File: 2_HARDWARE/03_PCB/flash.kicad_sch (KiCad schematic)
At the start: 8 parts, among them U15 W25Q128JVSIQ, U16 W25Q128JVSIQ

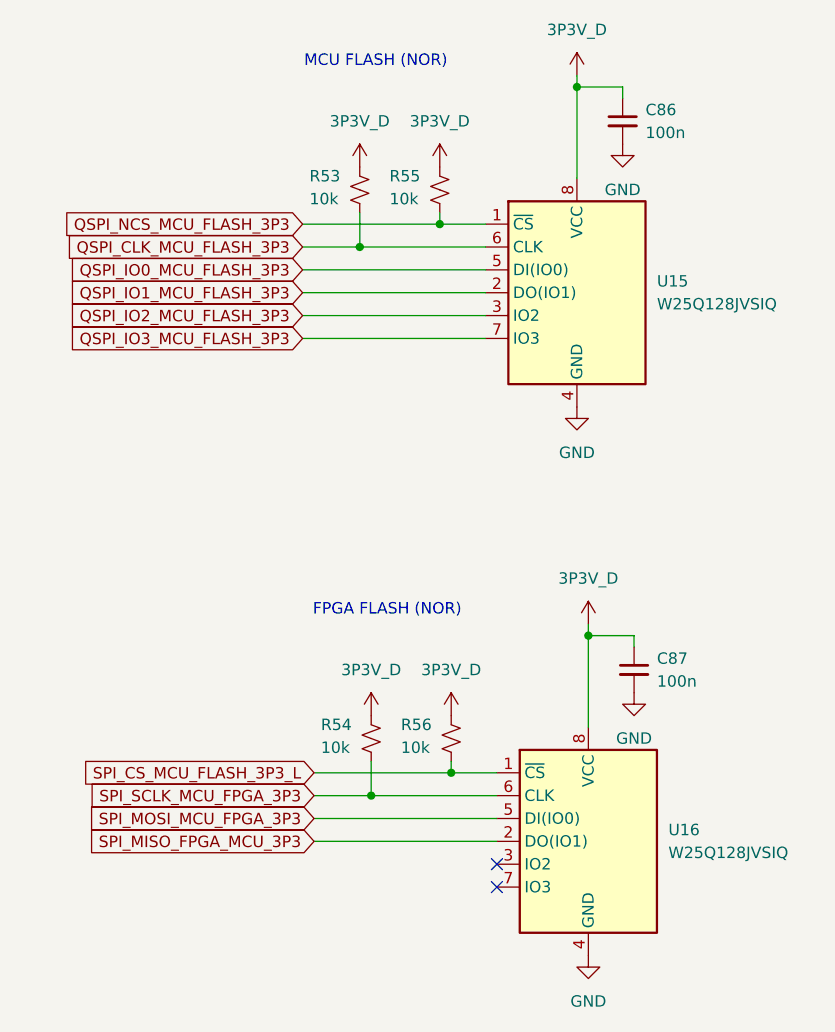
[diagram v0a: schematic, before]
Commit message: MINOR: Changed Boot Select Switches to Pull-Downs / Pull Up DNI and continued layout.
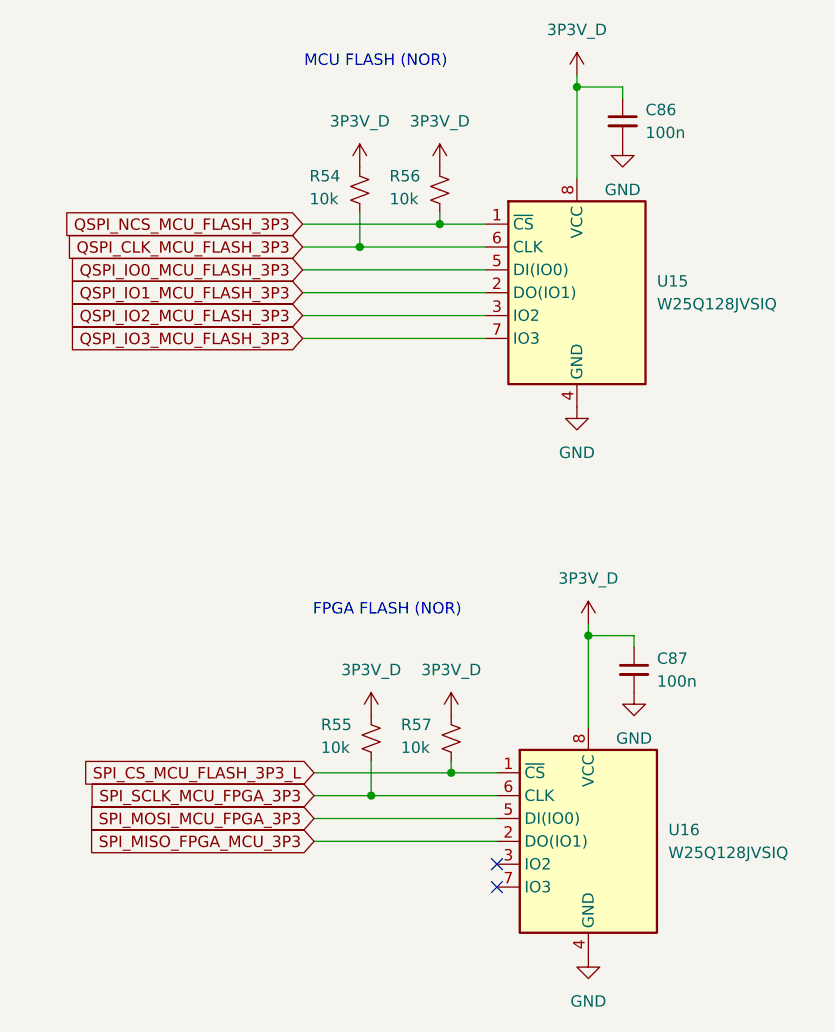
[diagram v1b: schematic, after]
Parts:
- renumbered R53 to R54, R54 to R55, R55 to R56, R56 to R57
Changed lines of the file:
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@@
+		(dnp no)
+		(fields_autoplaced yes)
+		(property "Reference" "#PWR0207"
+			(at 156.21 105.41 0)
+			(effects
+				(font
+					(size 1.27 1.27)
+				)
+				(hide yes)
+			)
+		)
+		(property "Value" "GND"
+			(at 156.21 104.14 0)
+			(effects
+				(font
+					(size 1.27 1.27)
+				)
+			)
+		)
+		(property "Footprint" ""
+			(at 156.21 99.06 0)
+			(effects
+				(font
+					(size 1.27 1.27)
+				)
+				(hide yes)
+			)
+		)
+		(property "Datasheet" ""
+			(at 156.21 99.06 0)
+			(effects
+				(font
+					(size 1.27 1.27)
+				)
+				(hide yes)
+			)
+		)
+		(property "Description" "Power symbol creates a global label with name \"GND\" , ground"
+			(at 156.21 99.06 0)
+			(effects
+				(font
+					(size 1.27 1.27)
+				)
+				(hide yes)
+			)
+		)
+		(pin "1"
+		)
+		(instances
+			(project "arb"
+				(path "/866ef9be-3b01-4288-a6e0-a2357aa17e50/3eaf535e-ef91-4de7-bf25-42486b2f88fe"
+					(reference "#PWR0207")
+					(unit 1)
+				)
+			)
+		)
+	)
+	(symbol
+		(lib_id "Device:R_Small_US")
+		(at 133.35 135.89 180)
+		(unit 1)
+		(exclude_from_sim no)
+		(in_bom yes)
+		(on_board yes)
+		(dnp no)
+		(property "Reference" "R55"
+			(at 127.762 134.366 0)
+			(effects
+				(font
+					(size 1.27 1.27)
+				)
+				(justify right)
+			)
+		)
+		(property "Value" "10k"
+			(at 127.762 136.906 0)
+			(effects
+				(font
+					(size 1.27 1.27)
+				)
+				(justify right)
+			)
+		)
+		(property "Footprint" "Resistor_SMD:R_0603_1608Metric"
+			(at 133.35 135.89 0)
+			(effects
+				(font
+					(size 1.27 1.27)
+				)
+				(hide yes)
+			)
+		)
+		(property "Datasheet" "~"
+			(at 133.35 135.89 0)
+			(effects
+				(font
+					(size 1.27 1.27)
+				)
+				(hide yes)
+			)
+		)
+		(property "Description" "Resistor, small US symbol"
+			(at 133.35 135.89 0)
+			(effects
+				(font
+					(size 1.27 1.27)
+				)
+				(hide yes)
+			)
+		)
+		(property "Part Number" "0603WAF1002T5E"
+			(at 133.35 135.89 0)
+			(effects
+				(font
+					(size 1.27 1.27)
+				)
+				(hide yes)
+			)
+		)
+		(property "LCSC" "C25804"
+			(at 133.35 135.89 0)
+			(effects
+				(font
+					(size 1.27 1.27)
+				)
+				(hide yes)
+			)
+		)
+		(pin "1"
+		)
+		(pin "2"
+		)
+		(instances
+			(project "arb"
+				(path "/866ef9be-3b01-4288-a6e0-a2357aa17e50/3eaf535e-ef91-4de7-bf25-42486b2f88fe"
+					(reference "R55")
+					(unit 1)
+				)
+			)
+		)
+	)
+	(symbol
+		(lib_id "power:GND")
+		(at 162.56 130.81 0)
+		(unit 1)
+		(exclude_from_sim no)
+		(in_bom yes)
+		(on_board yes)
 		(dnp no)
 		(fields_autoplaced yes)
 		(property "Reference" "#PWR0211"
-			(at 156.21 105.41 0)
-			(effects
-				(font
-					(size 1.27 1.27)
-				)
-				(hide yes)
-			)
-		)
-		(property "Value" "GND"
-			(at 156.21 104.14 0)
-			(effects
-				(font
-					(size 1.27 1.27)
-				)
-			)
-		)
-		(property "Footprint" ""
-			(at 156.21 99.06 0)
-			(effects
-				(font
-					(size 1.27 1.27)
-				)
-				(hide yes)
-			)
-		)
-		(property "Datasheet" ""
-			(at 156.21 99.06 0)
-			(effects
-				(font
-					(size 1.27 1.27)
-				)
-				(hide yes)
-			)
-		)
-		(property "Description" "Power symbol creates a global label with name \"GND\" , ground"
-			(at 156.21 99.06 0)
-			(effects
-				(font
-					(size 1.27 1.27)
-				)
-				(hide yes)
-			)
-		)
-		(pin "1"
-		)
-		(instances
-			(project "arb"
-				(path "/866ef9be-3b01-4288-a6e0-a2357aa17e50/3eaf535e-ef91-4de7-bf25-42486b2f88fe"
-					(reference "#PWR0211")
-					(unit 1)
-				)
-			)
-		)
-	)
-	(symbol
-		(lib_id "Device:R_Small_US")
-		(at 133.35 135.89 180)
-		(unit 1)
-		(exclude_from_sim no)
-		(in_bom yes)
-		(on_board yes)
-		(dnp no)
-		(property "Reference" "R54"
-			(at 127.762 134.366 0)
-			(effects
-				(font
-					(size 1.27 1.27)
-				)
-				(justify right)
-			)
-		)
-		(property "Value" "10k"
-			(at 127.762 136.906 0)
-			(effects
-				(font
-					(size 1.27 1.27)
-				)
-				(justify right)
-			)
-		)
-		(property "Footprint" "Resistor_SMD:R_0603_1608Metric"
-			(at 133.35 135.89 0)
-			(effects
-				(font
-					(size 1.27 1.27)
-				)
-				(hide yes)
-			)
-		)
-		(property "Datasheet" "~"
-			(at 133.35 135.89 0)
-			(effects
-				(font
-					(size 1.27 1.27)
-				)
-				(hide yes)
-			)
-		)
-		(property "Description" "Resistor, small US symbol"
-			(at 133.35 135.89 0)
-			(effects
-				(font
-					(size 1.27 1.27)
-				)
-				(hide yes)
-			)
-		)
-		(property "Part Number" "0603WAF1002T5E"
-			(at 133.35 135.89 0)
-			(effects
-				(font
-					(size 1.27 1.27)
-				)
-				(hide yes)
-			)
-		)
-		(property "LCSC" "C25804"
-			(at 133.35 135.89 0)
-			(effects
-				(font
-					(size 1.27 1.27)
-				)
-				(hide yes)
-			)
-		)
-		(pin "1"
-		)
-		(pin "2"
-		)
-		(instances
-			(project "arb"
-				(path "/866ef9be-3b01-4288-a6e0-a2357aa17e50/3eaf535e-ef91-4de7-bf25-42486b2f88fe"
-					(reference "R54")
-					(unit 1)
-				)
-			)
-		)
-	)
-	(symbol
-		(lib_id "power:GND")
-		(at 162.56 130.81 0)
-		(unit 1)
-		(exclude_from_sim no)
-		(in_bom yes)
-		(on_board yes)
-		(dnp no)
-		(fields_autoplaced yes)
-		(property "Reference" "#PWR0215"
 			(at 162.56 137.16 0)
 			(effects
@@
 			(project "arb"
 				(path "/866ef9be-3b01-4288-a6e0-a2357aa17e50/3eaf535e-ef91-4de7-bf25-42486b2f88fe"
-					(reference "#PWR0215")
+					(reference "#PWR0211")
 					(unit 1)
 				)
@@
 		(dnp no)
 		(fields_autoplaced yes)
-		(property "Reference" "#PWR0210"
+		(property "Reference" "#PWR0206"
 			(at 156.21 66.04 0)
 			(effects
@@
 			(project "arb"
 				(path "/866ef9be-3b01-4288-a6e0-a2357aa17e50/3eaf535e-ef91-4de7-bf25-42486b2f88fe"
-					(reference "#PWR0210")
+					(reference "#PWR0206")
 					(unit 1)
 				)
@@
 		(dnp no)
 		(fields_autoplaced yes)
-		(property "Reference" "#PWR0214"
+		(property "Reference" "#PWR0210"
 			(at 161.29 76.2 0)
 			(effects
@@
 			(project "arb"
 				(path "/866ef9be-3b01-4288-a6e0-a2357aa17e50/3eaf535e-ef91-4de7-bf25-42486b2f88fe"
-					(reference "#PWR0214")
+					(reference "#PWR0210")
 					(unit 1)
 				)
@@
 		(on_board yes)
 		(dnp no)
-		(property "Reference" "R56"
+		(property "Reference" "R57"
 			(at 136.652 134.366 0)
 			(effects
@@
 			(project "arb"
 				(path "/866ef9be-3b01-4288-a6e0-a2357aa17e50/3eaf535e-ef91-4de7-bf25-42486b2f88fe"
-					(reference "R56")
+					(reference "R57")
 					(unit 1)
 				)
@@
 		(dnp no)
 		(fields_autoplaced yes)
-		(property "Reference" "#PWR0212"
+		(property "Reference" "#PWR0208"
 			(at 157.48 127 0)
 			(effects
@@
 			(project "arb"
 				(path "/866ef9be-3b01-4288-a6e0-a2357aa17e50/3eaf535e-ef91-4de7-bf25-42486b2f88fe"
-					(reference "#PWR0212")
+					(reference "#PWR0208")
 					(unit 1)
 				)
@@
 		(on_board yes)
 		(dnp no)
-		(property "Reference" "R53"
+		(property "Reference" "R54"
 			(at 126.492 73.406 0)
 			(effects
@@
 			(project "arb"
 				(path "/866ef9be-3b01-4288-a6e0-a2357aa17e50/3eaf535e-ef91-4de7-bf25-42486b2f88fe"
-					(reference "R53")
+					(reference "R54")
 					(unit 1)
 				)
@@
 		(on_board yes)
 		(dnp no)
-		(property "Reference" "R55"
+		(property "Reference" "R56"
 			(at 135.382 73.406 0)
 			(effects
@@
 			(project "arb"
 				(path "/866ef9be-3b01-4288-a6e0-a2357aa17e50/3eaf535e-ef91-4de7-bf25-42486b2f88fe"
-					(reference "R55")
+					(reference "R56")
 					(unit 1)
 				)
@@
 		(dnp no)
 		(fields_autoplaced yes)
-		(property "Reference" "#PWR0209"
+		(property "Reference" "#PWR0205"
 			(at 142.24 137.16 0)
 			(effects
@@
 			(project "arb"
 				(path "/866ef9be-3b01-4288-a6e0-a2357aa17e50/3eaf535e-ef91-4de7-bf25-42486b2f88fe"
-					(reference "#PWR0209")
+					(reference "#PWR0205")
 					(unit 1)
 				)
@@
 		(dnp no)
 		(fields_autoplaced yes)
-		(property "Reference" "#PWR0207"
+		(property "Reference" "#PWR0203"
 			(at 133.35 137.16 0)
 			(effects
@@
 			(project "arb"
 				(path "/866ef9be-3b01-4288-a6e0-a2357aa17e50/3eaf535e-ef91-4de7-bf25-42486b2f88fe"
-					(reference "#PWR0207")
+					(reference "#PWR0203")
 					(unit 1)
 				)
@@
 		(dnp no)
 		(fields_autoplaced yes)
-		(property "Reference" "#PWR0213"
+		(property "Reference" "#PWR0209"
 			(at 157.48 166.37 0)
 			(effects
@@
 			(project "arb"
 				(path "/866ef9be-3b01-4288-a6e0-a2357aa17e50/3eaf535e-ef91-4de7-bf25-42486b2f88fe"
-					(reference "#PWR0213")
+					(reference "#PWR0209")
 					(unit 1)
 				)
@@
 		(dnp no)
 		(fields_autoplaced yes)
-		(property "Reference" "#PWR0206"
+		(property "Reference" "#PWR0202"
 			(at 132.08 76.2 0)
 			(effects
@@
 			(project "arb"
 				(path "/866ef9be-3b01-4288-a6e0-a2357aa17e50/3eaf535e-ef91-4de7-bf25-42486b2f88fe"
-					(reference "#PWR0206")
+					(reference "#PWR0202")
 					(unit 1)
 				)
@@
 		(dnp no)
 		(fields_autoplaced yes)
-		(property "Reference" "#PWR0208"
+		(property "Reference" "#PWR0204"
 			(at 140.97 76.2 0)
 			(effects
@@
 			(project "arb"
 				(path "/866ef9be-3b01-4288-a6e0-a2357aa17e50/3eaf535e-ef91-4de7-bf25-42486b2f88fe"
-					(reference "#PWR0208")
-					(unit 1)
-				)
+					(reference "#PWR0204")
+					(unit 1)
+				)

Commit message: FEAT: Fixed Silkscreen + Resolved all DRC Errors.
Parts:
- U15, U16: footprint Package_SO:SOIC-8_5.23x5.23mm_P1.27mm -> Package_SO:SOIC-8_5.3x5.3mm_P1.27mm
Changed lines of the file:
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@@
 			)
 		)
-		(property "Footprint" "Package_SO:SOIC-8_5.23x5.23mm_P1.27mm"
+		(property "Footprint" "Package_SO:SOIC-8_5.3x5.3mm_P1.27mm"
 			(at 157.48 147.32 0)
 			(effects
@@
 			)
 		)
-		(property "Footprint" "Package_SO:SOIC-8_5.23x5.23mm_P1.27mm"
+		(property "Footprint" "Package_SO:SOIC-8_5.3x5.3mm_P1.27mm"
 			(at 156.21 86.36 0)
 			(effects
